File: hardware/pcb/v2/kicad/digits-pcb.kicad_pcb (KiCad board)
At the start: 2 copper layers, 76.2 x 56.9 mm, 70 parts, among them J1 Conn_02x20_Odd_Even, J3 VIN_BARREL_PIGTAIL, J4 Conn_01x07, J6 Conn_01x02, J7 Screw_Terminal_01x02, J8 Conn_01x04, J9 Conn_01x03, U1 LM2596S-5, U2 DRV8871DDAR, U3 RP2040, U4 W25Q16JVSSIQ, U5 AMS1117-3.3, U6 TLV320AIC3104IRHBR, U7 XC6206P182MR, Y1 ABM8-272-T3

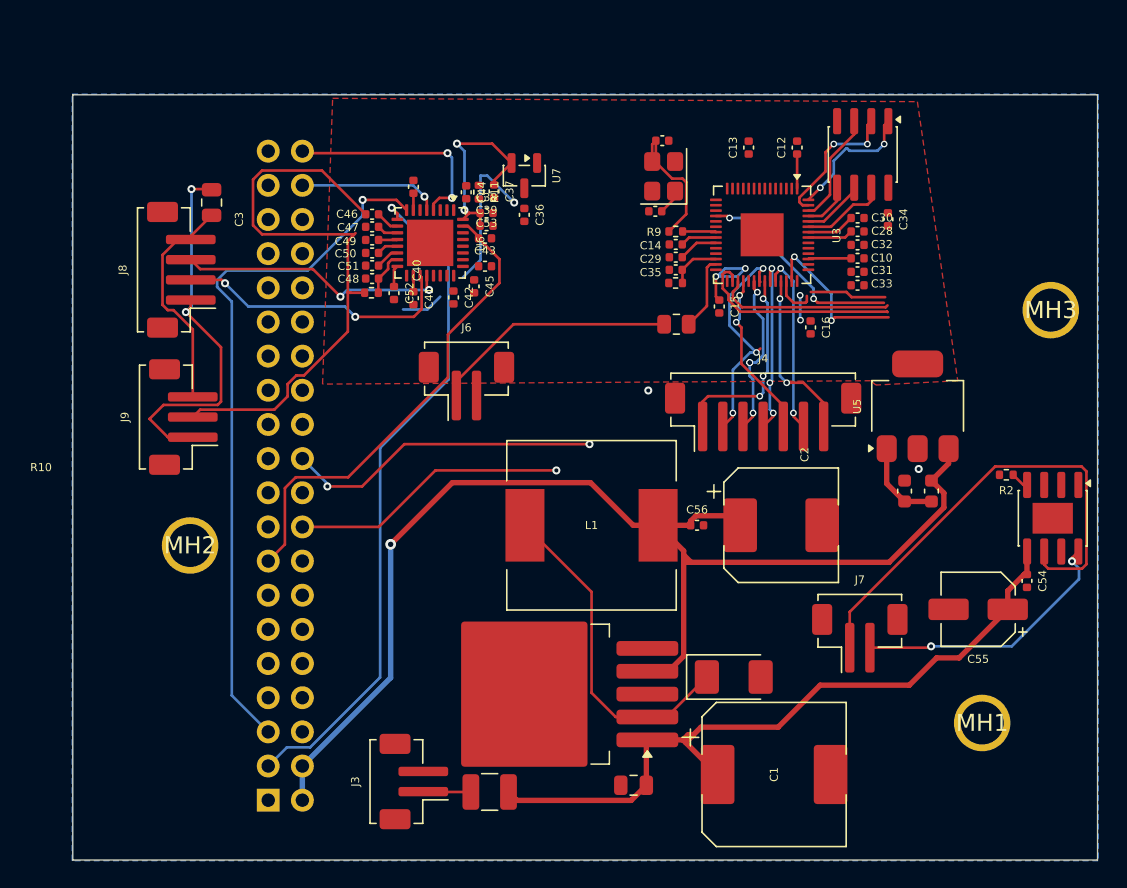
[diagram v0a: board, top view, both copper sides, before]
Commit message: fix(hardware): fix component placement DRC violations + mounting hole footprints
Fix empty footprint names on MH1-MH3 (caused freerouter SES import failures).
Move displaced decaps (C12, C15, C34, C54, C55) near their target IC pins.
Relocate U2 (DRV8871) near power section with C54/C55/R2 cluster.
Restore SW1 hook switch to enclosure-dictated position.
Delete dangling CODEC_SCL and +12V trace stubs.
All 7 placement checkers pass (crystal borderline, pre-existing).
DRC down to 4 starved thermals (fixed via solid pad connections).
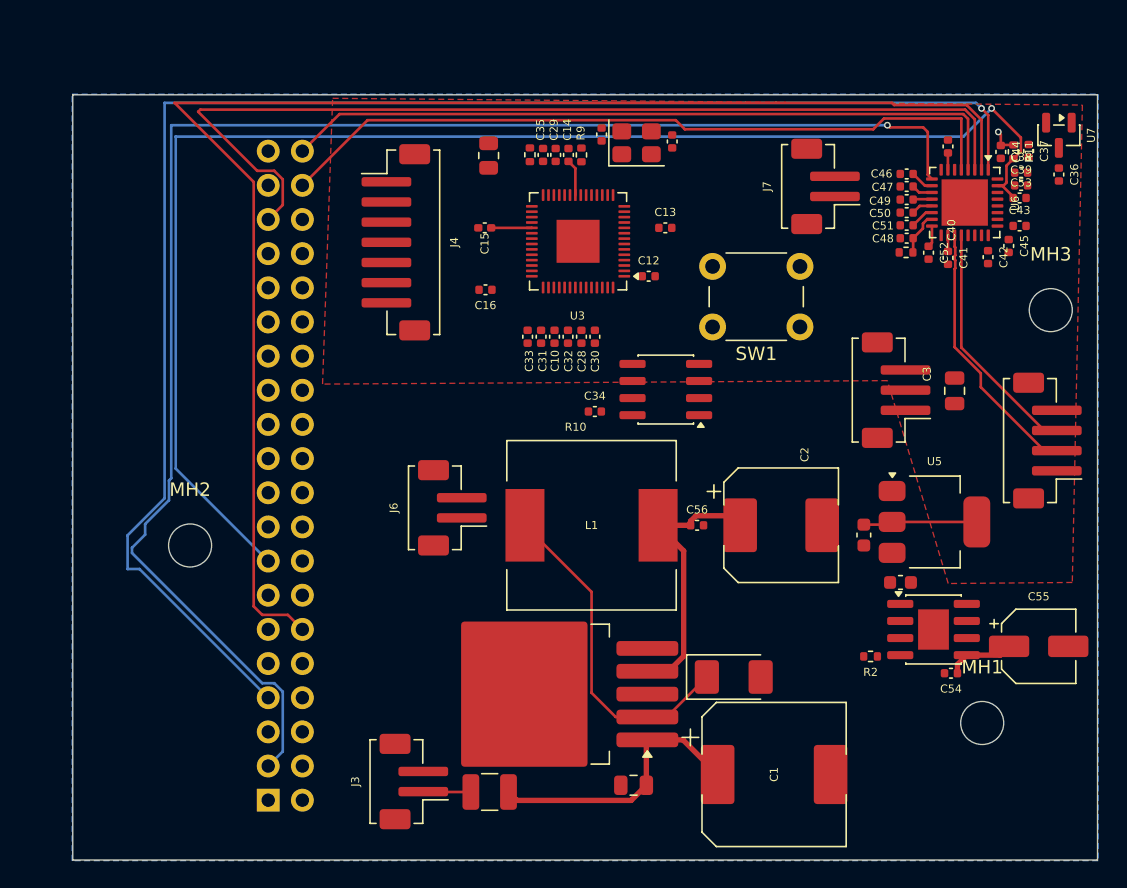
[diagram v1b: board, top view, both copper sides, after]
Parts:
- added SW1: SW_Push, Button_Switch_THT:SW_PUSH_6mm, B.Cu at (68.8, 31.7)
- MH1, MH2, MH3: value MountingHole_3.2mm -> MountingHole; footprint (none) -> MountingHole:MountingHole_3.2mm_M3
- moved J8 65.6 mm to (87.2, 40.2)
- moved C3 57.0 mm to (80.2, 36.5), turned to 90 degrees
- moved J9 53.0 mm to (75.9, 36.4)
- moved C46 39.9 mm to (76.7, 20.3)
- moved C47 39.9 mm to (76.7, 21.3)
- moved C48 39.9 mm to (76.7, 25.1)
- moved C49 39.9 mm to (76.7, 22.2)
- moved C50 39.9 mm to (76.7, 23.2)
- moved C51 39.9 mm to (76.7, 24.2)
- moved C53 39.9 mm to (85.1, 22.1)
- moved C36 39.9 mm to (88.0, 20.4)
- moved C37 39.9 mm to (85.8, 18.6)
- moved C39 39.9 mm to (85.2, 21.2)
- moved C40 39.9 mm to (79.8, 18.3)
- moved C41 39.9 mm to (79.8, 26.6)
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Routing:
- net CODEC_MCLK: track 0.00 -> 115.9 mm, vias 0 -> 1
- net CODEC_BCLK: track 0.00 -> 108.4 mm
- net CODEC_WCLK: track 0.00 -> 73.7 mm
- net +5V: track 92.5 -> 20.6 mm, vias 1 -> 0
- net CODEC_RESET: track 35.7 -> 105.2 mm, vias 0 -> 1
- net CODEC_SDA: track 50.9 -> 114.6 mm
- net CODEC_SCL: track 52.7 -> 0.00 mm, vias 1 -> 0
- net MIC_FROM_SW: track 45.0 -> 0.00 mm
- net CODEC_DOUT: track 10.5 -> 55.4 mm, vias 1 -> 0
- net CODEC_DIN: track 16.3 -> 54.6 mm, vias 2 -> 0
- net BELL_A: track 36.2 -> 0.00 mm
- net MIC_HOT: track 29.2 -> 0.00 mm, vias 2 -> 0
- net +12V: track 54.7 -> 25.7 mm
- net SWD_SWCLK: track 23.6 -> 0.00 mm, vias 2 -> 0
- net SWD_SWDIO: track 20.6 -> 0.00 mm, vias 1 -> 0
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
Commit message: feat(hardware): freerouter pass + locked +3V3 stubs, 0 DRC violations
Route 23 locked +3V3 stubs from IC/decap pads into pour areas to protect
thermal relief spokes from freerouter interference. Lock all +3V3 traces
on F.Cu and B.Cu. Run freerouter for remaining signal routing. Fix 5
starved thermal violations: solid pad connections on edge pads, GND via
replacement on U6.6, manual spoke routing on remaining pads.
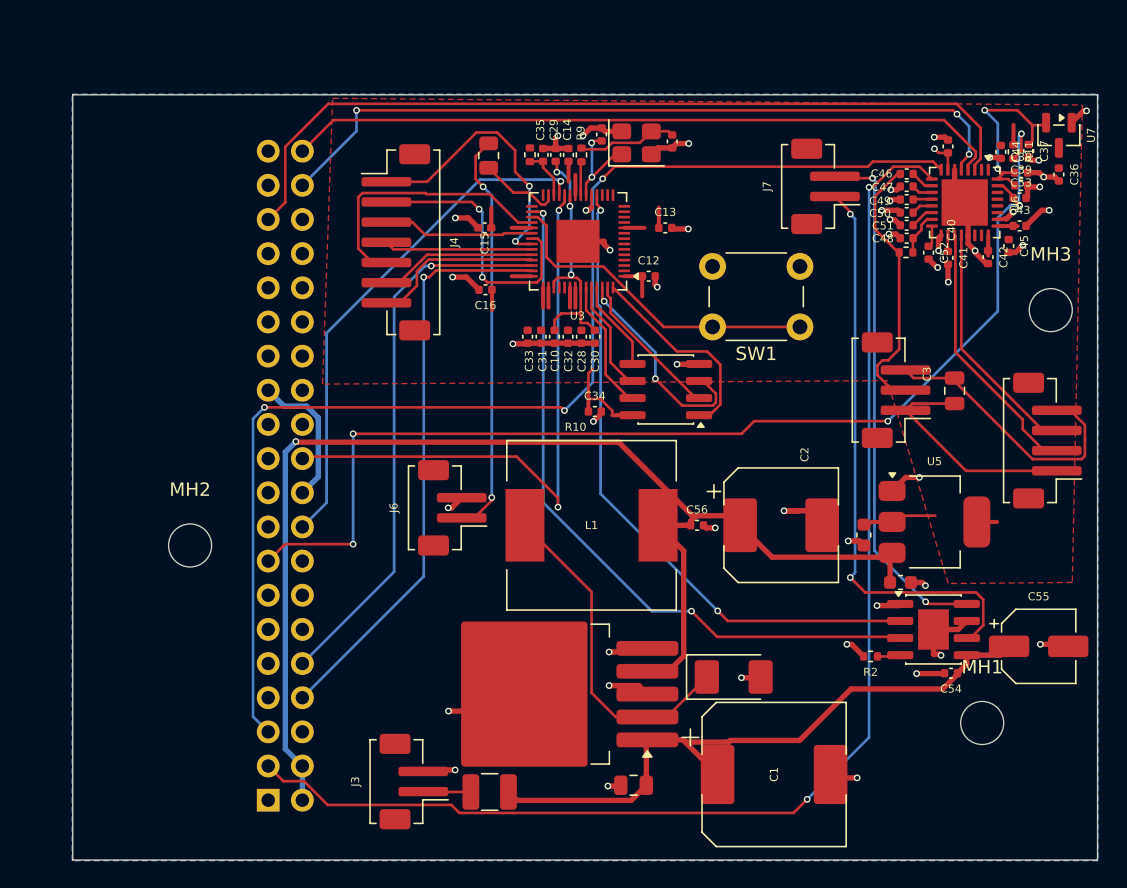
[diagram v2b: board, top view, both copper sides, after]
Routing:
- net CODEC_MCLK: track 115.9 -> 0.00 mm, vias 1 -> 0
- net GND: track 0.00 -> 115.8 mm, vias 0 -> 48
- net CODEC_BCLK: track 108.4 -> 0.00 mm
- net CODEC_SCL: track 0.00 -> 91.7 mm, vias 0 -> 3
- net +5V: track 20.6 -> 94.5 mm, vias 0 -> 1
- net RINGER_IN1: track 0.00 -> 53.1 mm, vias 0 -> 2
- net RINGER_IN2: track 0.00 -> 48.7 mm, vias 0 -> 2
- net SWD_SWCLK: track 0.00 -> 44.4 mm, vias 0 -> 2
- net UART_TX_PI: track 0.00 -> 43.3 mm, vias 0 -> 1
- net BELL_A: track 0.00 -> 43.2 mm, vias 0 -> 2
- net UART_RX_PI: track 0.00 -> 41.3 mm, vias 0 -> 1
- net BELL_B: track 0.00 -> 39.2 mm, vias 0 -> 2
- net SWD_SWDIO: track 0.00 -> 38.4 mm, vias 0 -> 1
- net LED_A: track 0.00 -> 30.2 mm, vias 0 -> 2
- net +3V3: track 18.7 -> 45.0 mm
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
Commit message: feat(hardware): extend board outline 5mm north for routing clearance
Move top edge from y=14.45 to y=9.45, giving more room for codec I2S
traces that were slicing through the F.Cu +3V3 pour and creating
disconnected copper islands.
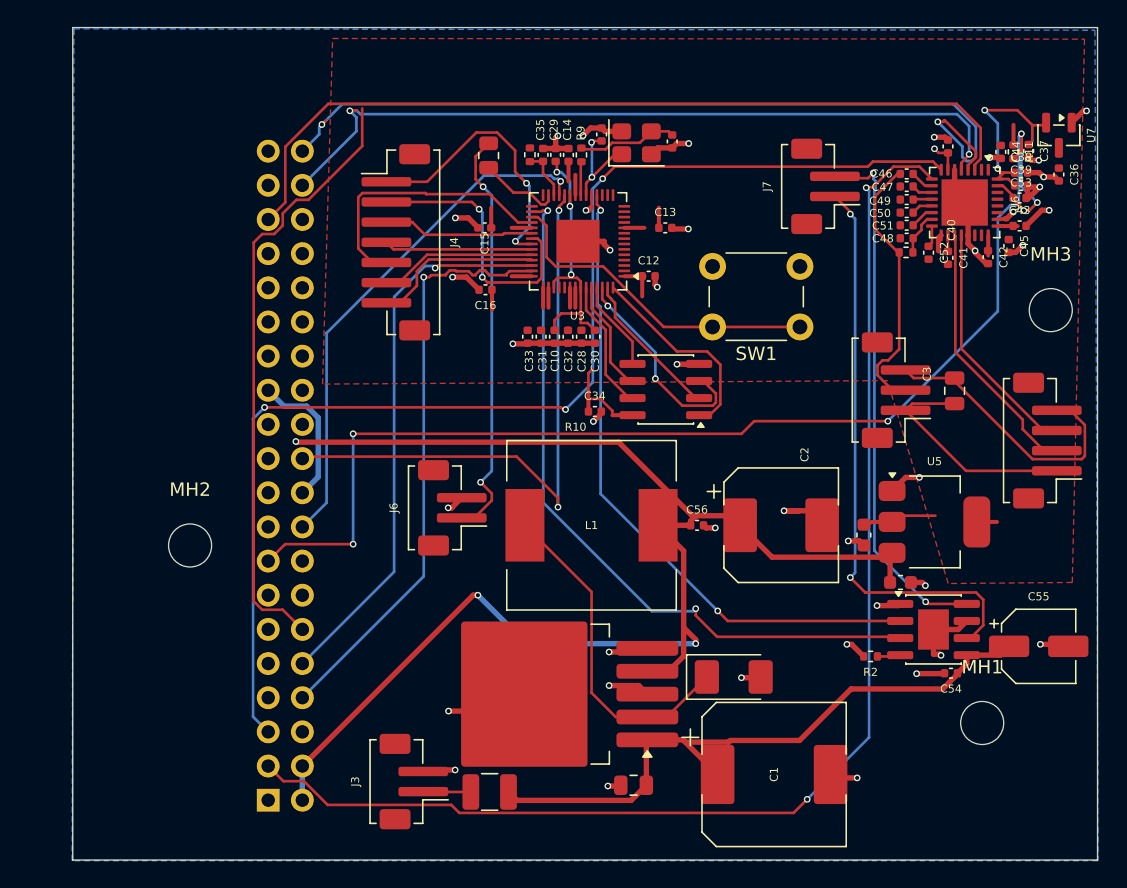
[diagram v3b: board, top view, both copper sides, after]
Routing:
- net CODEC_BCLK: track 0.00 -> 45.5 mm
- net +5V: track 94.5 -> 107.1 mm, vias 1 -> 3
- net CODEC_DIN: track 53.6 -> 65.3 mm, vias 0 -> 2
- net CODEC_RESET: track 85.6 -> 93.4 mm, vias 5 -> 6
- net GND: track 115.8 -> 109.9 mm, vias 48 -> 40
- net CODEC_DOUT: track 56.8 -> 57.9 mm, vias 3 -> 2
- net RINGER_IN1: track 53.1 -> 54.2 mm
- net UART_TX_PI: track 43.3 -> 44.0 mm
- net LED_A: track 30.2 -> 30.9 mm
- net BELL_B: track 39.2 -> 39.8 mm
- net SWD_SWCLK: track 44.4 -> 44.9 mm
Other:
- board size 76.2 x 56.9 mm -> 76.2 x 61.9 mm

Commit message: feat(hardware): PCB v2 checkpoint after board extension + routing pass
Checkpoint after extending the board 5mm north and continued routing
work. 133 segments added / 43 removed against prior checkpoint.
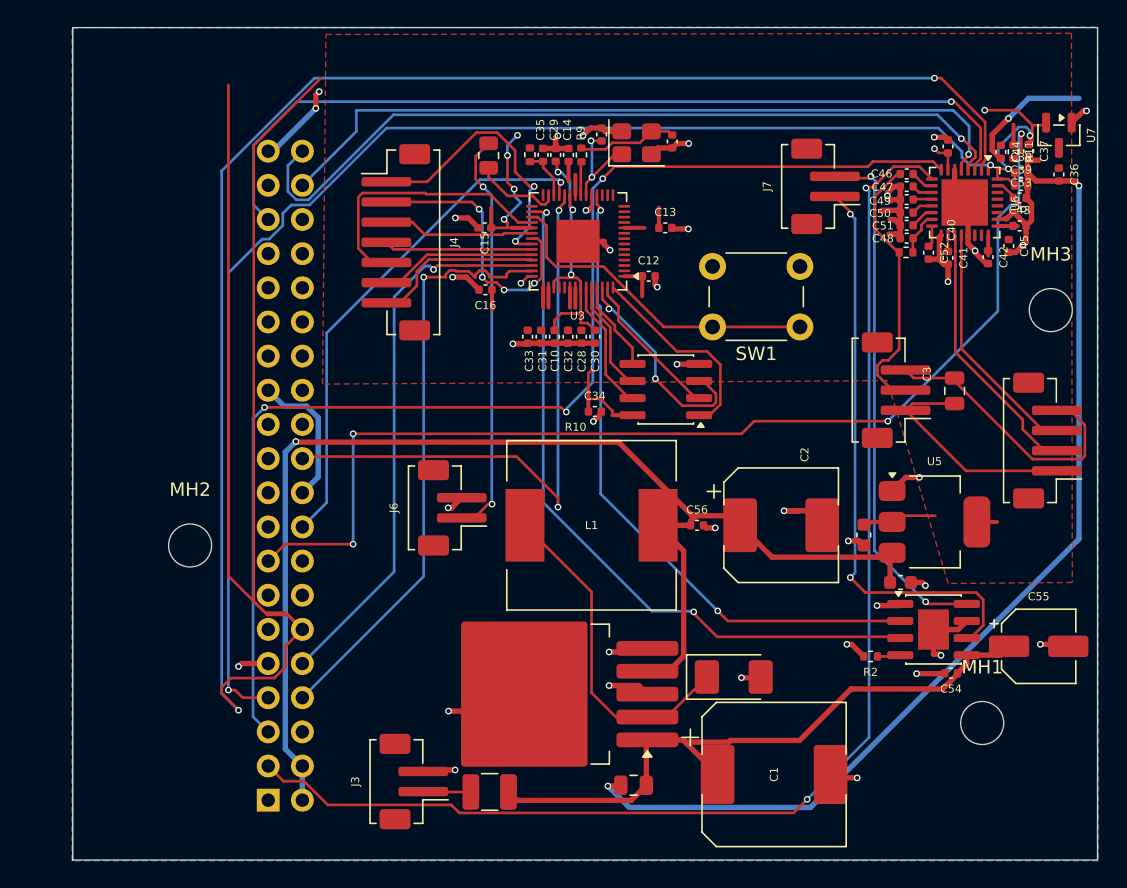
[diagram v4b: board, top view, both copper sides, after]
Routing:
- net CODEC_BCLK: track 45.5 -> 205.3 mm, vias 0 -> 2
- net GND: track 109.9 -> 215.5 mm, vias 40 -> 41
- net CODEC_MCLK: track 0.00 -> 97.7 mm, vias 0 -> 2
- net +5V: track 107.1 -> 94.5 mm, vias 3 -> 1
- net +3V3: track 45.0 -> 55.2 mm, vias 1 -> 6
- net CODEC_RESET: track 93.4 -> 86.4 mm, vias 6 -> 5
- net CODEC_DIN: track 65.3 -> 60.1 mm, vias 2 -> 1
- net CODEC_WCLK: track 63.0 -> 65.5 mm, vias 0 -> 1
- net /codec/+1V8: track 14.9 -> 16.7 mm, vias 2 -> 3
- net CODEC_DOUT: track 57.9 -> 56.8 mm, vias 2 -> 1
- net RINGER_IN1: track 54.2 -> 53.6 mm
- net UART_TX_PI: track 44.0 -> 44.6 mm
- net SWD_SWCLK: track 44.9 -> 44.4 mm
- net LED_A: track 30.9 -> 30.4 mm
- net KP_COL1: track 20.5 -> 20.9 mm, vias 2 -> 4

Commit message: feat(hardware): PCB v2 checkpoint, U3.19 GND stitched, 0 unconnected
Added L-shaped F.Cu stub from U3.19 (TESTEN) exiting north through
the pin-row gap, out to a stitching via at (54.7, 21.0) that hops to
the B.Cu GND pour. Cleaned up 24 orphaned segments/vias left over
from prior freerouter passes.

State: 0 unconnected items; 2 dangling stubs remain (+3V3 via at
45,30.21 and GND track at 78.5,28.21); all other violations are
cosmetic (silk + library drift).
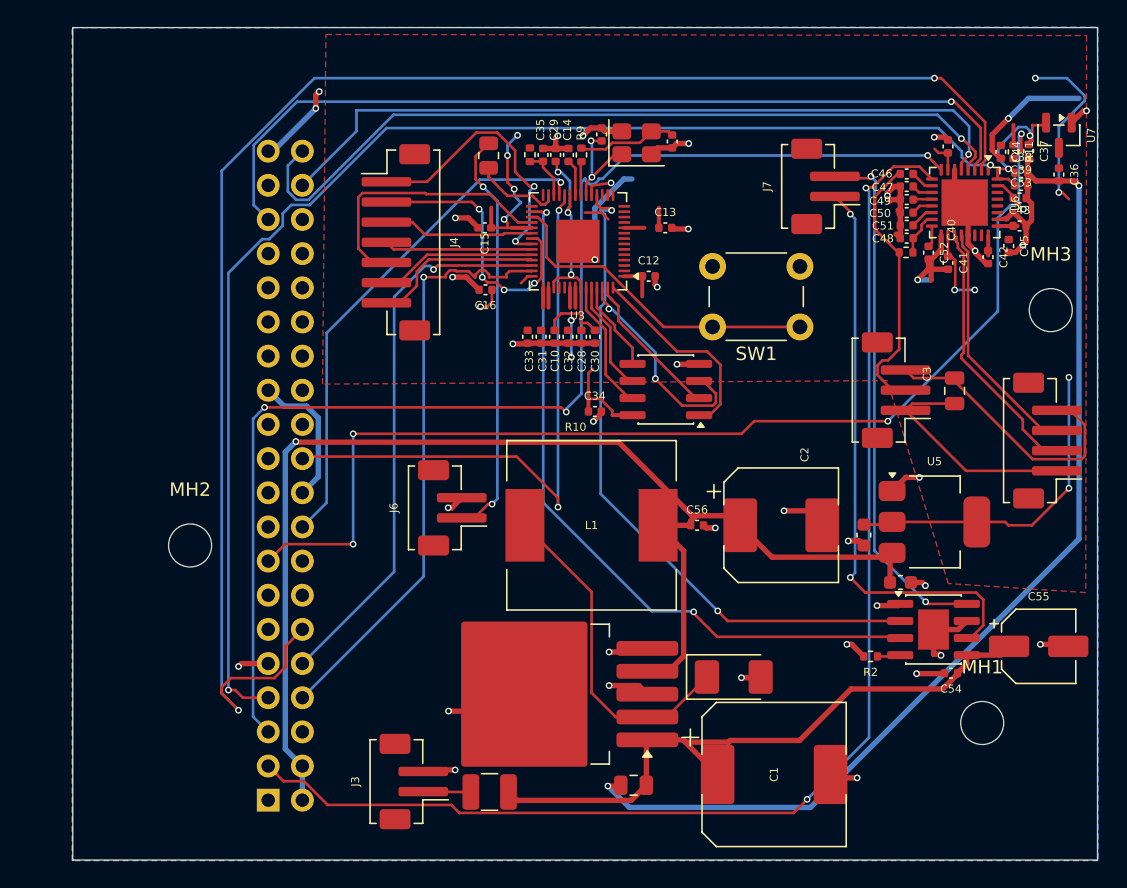
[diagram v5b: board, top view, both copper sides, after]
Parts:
- moved C41 0.37 mm to (79.8, 26.9)
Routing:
- net CODEC_BCLK: track 205.3 -> 116.2 mm
- net +3V3: track 55.2 -> 95.7 mm, vias 6 -> 13
- net GND: track 215.5 -> 220.3 mm
- net /codec/+1V8: track 16.7 -> 12.7 mm, vias 3 -> 2
- net RINGER_IN2: track 48.7 -> 50.3 mm
- net CODEC_SCL: track 91.9 -> 93.6 mm

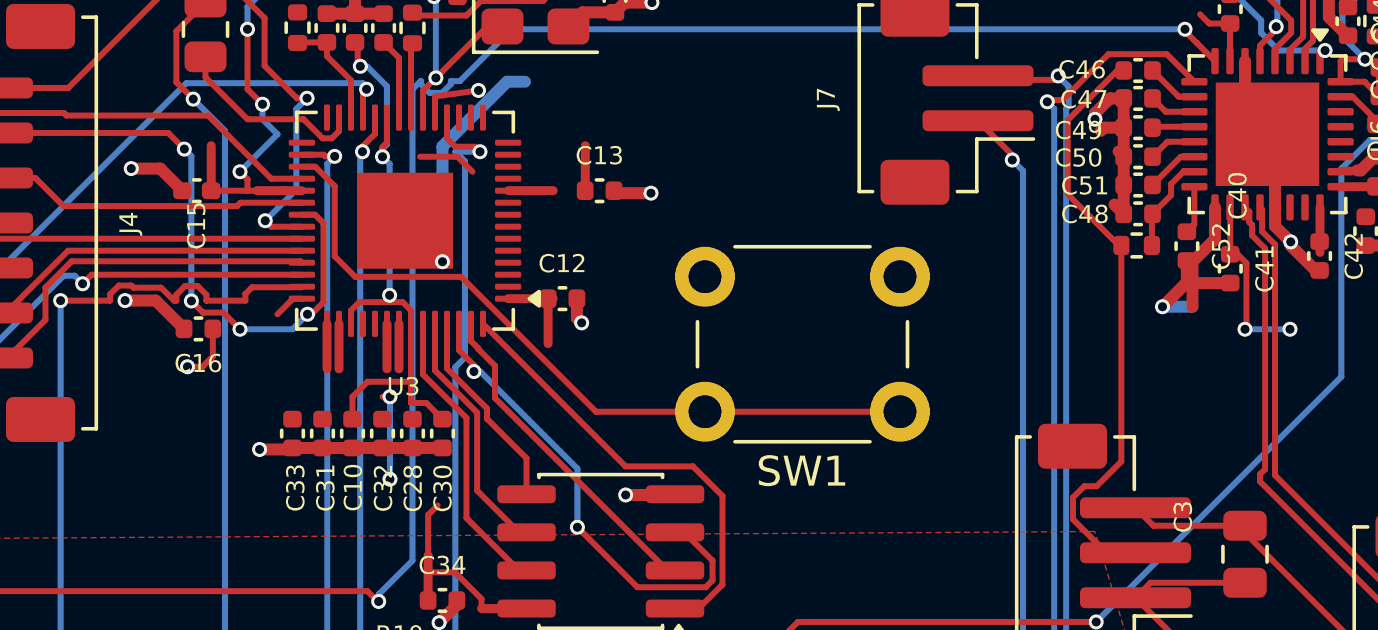
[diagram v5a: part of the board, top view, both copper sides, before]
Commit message: fix(hardware): delete 2 dangling stubs, DRC clean of all connectivity
Removed +3V3 dangling via at (45.0, 30.21) and GND dangling F.Cu
track at (78.5, 28.21). Board now has 0 unconnected, 0 dangling,
0 clearance violations; only silk and library-drift cosmetics remain.
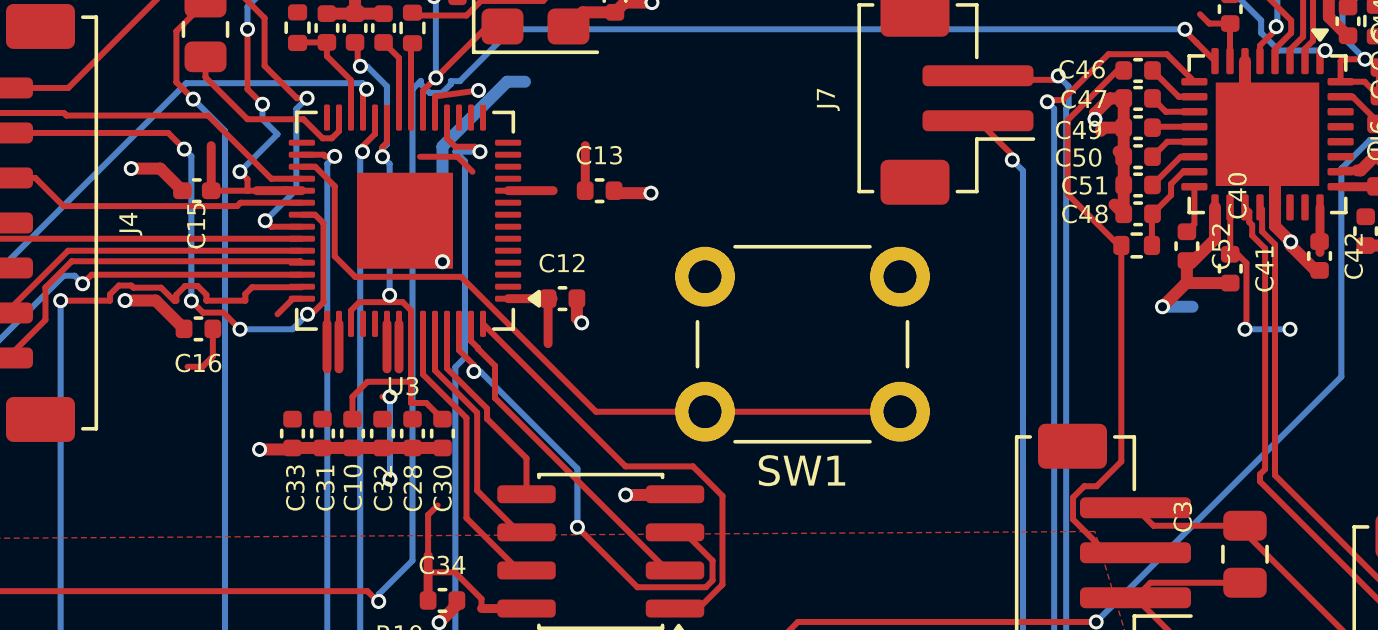
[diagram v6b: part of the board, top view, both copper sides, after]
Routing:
- net GND: track 220.3 -> 218.8 mm
- net +3V3: vias 13 -> 12
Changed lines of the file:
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@@
-	)
-	(via
-		(at 45 30.21)
-		(size 0.5)
-		(drill 0.3)
-		(layers "F.Cu" "B.Cu")
-		(net "+3V3")
 	)
 	(via
@@
 		(width 0.4)
 		(layer "F.Cu")
-		(net "GND")
-	)
-	(segment
-		(start 78.5 28.21)
-		(end 78.5 26.71)
-		(width 0.4)
-		(layer "F.Cu")
